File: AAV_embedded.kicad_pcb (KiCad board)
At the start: 4 copper layers, 168.2 x 114.7 mm, 84 parts, among them J1 JTAG_SWD_CONN, J10 DRV_HIGH_C2, J11 DRV_LOW_C2, J12 DRV_HIGH_C3, J13 DRV_LOW_C3, J14 DRV_LOW_C1, J15 Brake/FwRev, J16 5v_in, J17 3.3v_in, J18 12v_in, J2 Raspberry_Pi_4, J21 CAN, J23 5v_rail, J24 3.3v_rail, J25 12v_rail, J26 GND_rail, J27 12v_rail_f, J28 3.3v_rail_f, J29 5v_rail_f, J3 USB_C_Receptacle_USB2.0_14P, J30 GND_rail_f, J5 THR_EN_JMP, J6 Conn_01x07, J7 Conn_01x05, J8 Throttle Connector, J9 DRV_HIGH_C1, SW10 SW_DIP_x02, SW2 IO_EXT_ADDR, SW3 SW_DIP_x03, SW4 5v_USB_EN, SW5 THR_EN, SW6 ~{RESET_uMOD}, SW7 ~{BOOT_uMOD}, SW8 ~{RESET_BRK}, SW9 ~{RESET_STR}, U1 DAC101C081CIMK, U2 PCA9555D, U3 74AHC1G08, U5 FXMA108, U6 MCP2515-xSO, U7 SN65HVD230, Y1 16MHz

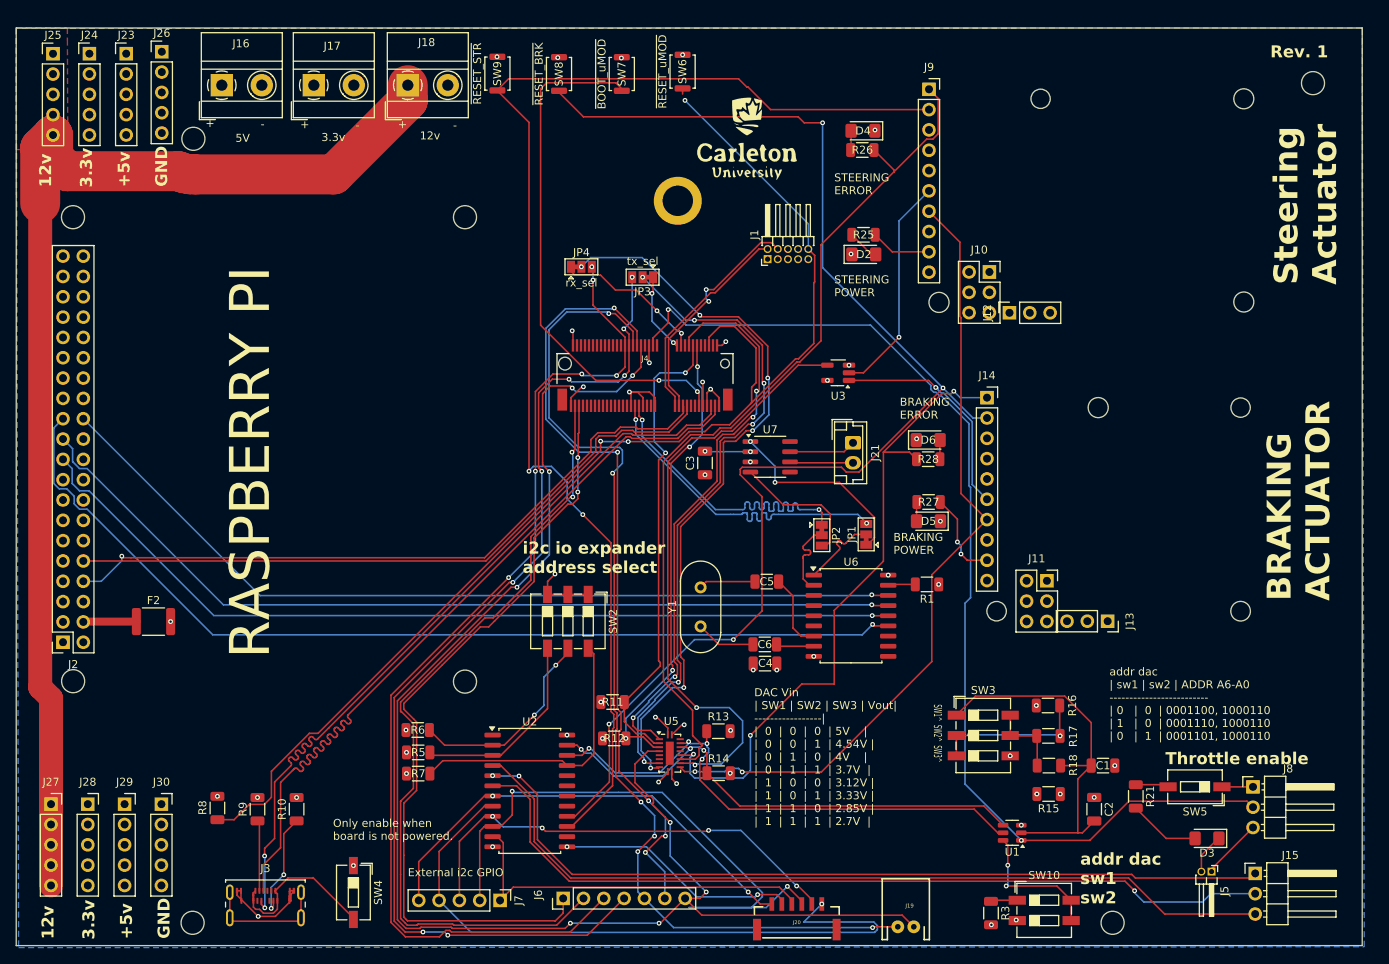
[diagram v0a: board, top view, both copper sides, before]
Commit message: Review and fixes from reliability and safety team
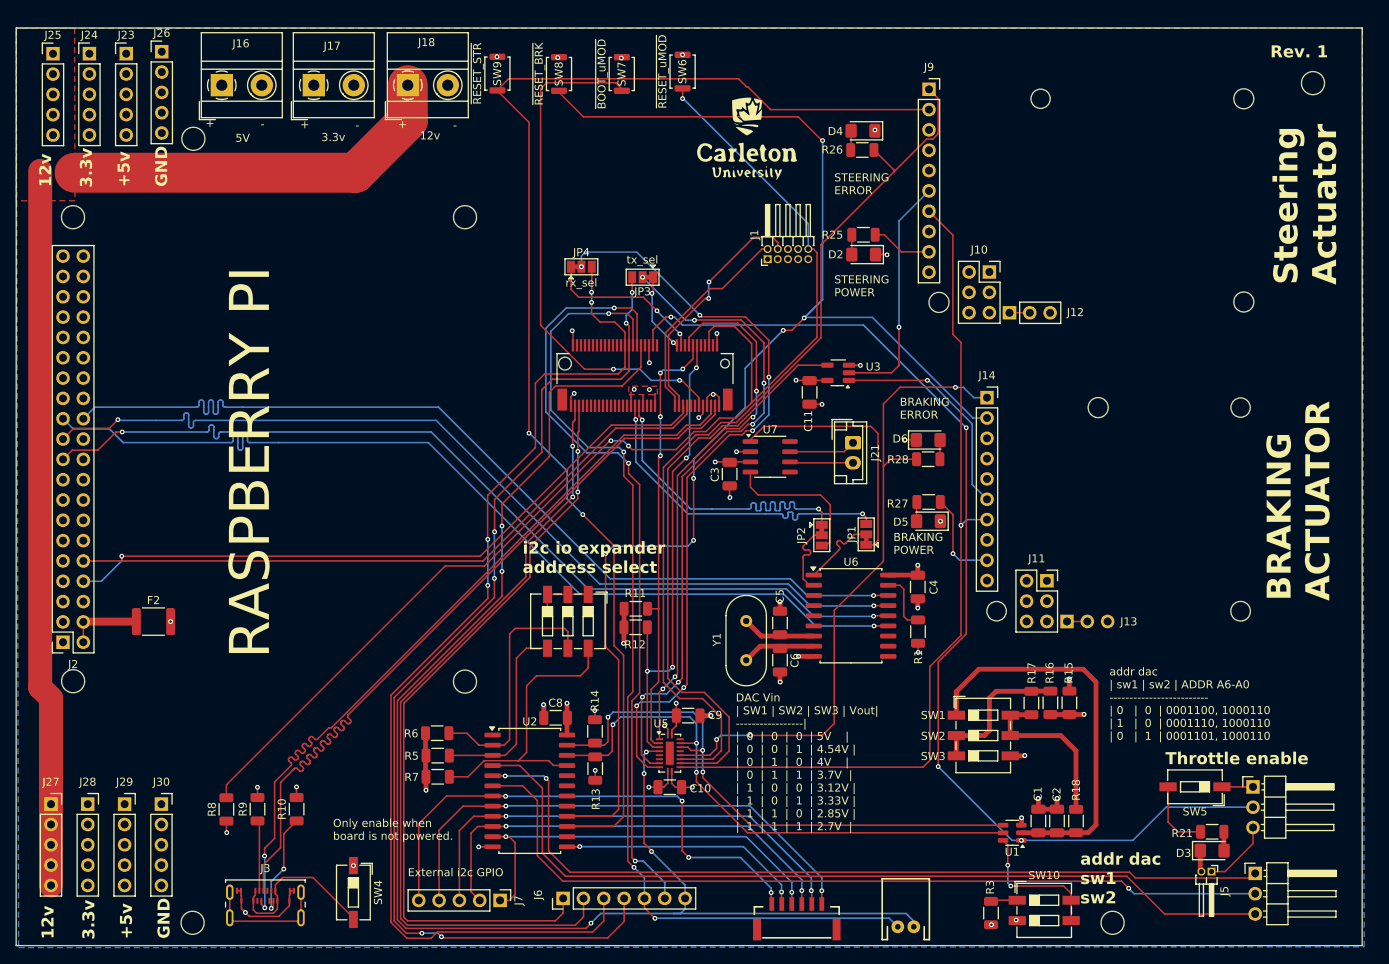
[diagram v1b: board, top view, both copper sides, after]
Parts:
- removed ?: , SparkFun-Hardware:STAND-OFF-REFLOW-M2.5
- added C10: 0.1uF, Capacitor_SMD:C_1206_3216Metric, F.Cu at (129.7, 138.1)
- added C11: 0.1uF, Capacitor_SMD:C_1206_3216Metric, F.Cu at (147.1, 88.7)
- added C8: 0.1uF, Capacitor_SMD:C_1206_3216Metric, F.Cu at (115.4, 129.4)
- added C9: 0.1uF, Capacitor_SMD:C_1206_3216Metric, F.Cu at (131.9, 129.1)
- Y1: footprint Crystal:Crystal_HC49-4H_Vertical -> Crystal:Crystal_HC18-U_Vertical
- moved C4 21.4 mm to (160.7, 113.0), turned to -90 degrees
- moved R14 16.3 mm to (120.3, 131.1), turned to 90 degrees
- moved R13 16.1 mm to (120.3, 135.7), turned to -90 degrees
- moved R12 14.1 mm to (125.4, 118.1)
- moved R11 12.0 mm to (125.4, 115.8)
- moved R15 11.7 mm to (179.6, 127.5), turned to -90 degrees
- moved C1 10.6 mm to (175.7, 142.3), turned to -90 degrees
- moved R21 10.5 mm to (197.4, 143.6), turned to 0 degrees
- moved R18 7.71 mm to (180.4, 142.3), turned to 90 degrees
- moved R1 6.01 mm to (160.7, 118.6), turned to 90 degrees
- moved Y1 5.74 mm to (139.2, 117.3), turned to -90 degrees
- moved C5 5.43 mm to (143.4, 117.5), turned to 90 degrees
- moved J13 5.08 mm to (179.3, 117.3), turned to 90 degrees
- moved C2 4.88 mm to (178.1, 142.3)
- moved R17 4.63 mm to (174.8, 127.5), turned to -90 degrees
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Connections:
- net Net-(D3-A) renamed /THR_STAT_K
- net Net-(D3-K) renamed /THR_STAT_A
- net Net-(R16-Pad1) renamed /SW2
- net Net-(R21-Pad1) renamed /THR_STAT_SW
- net Net-(U1-ADR0) renamed /DAC_ADR0
- net Net-(U2-A0) renamed /IO_EXP_A0
- net Net-(U2-A1) renamed /IO_EXP_A1
- net Net-(U2-A2) renamed /IO_EXP_A2
- net Net-(U6-~{RESET}) renamed /connectors/RESET
- C5 pad 1: Net-(U6-OSC2) -> /connectors/XTAL_2
- C5 pad 2: Net-(C5-Pad2) -> GND
- C6 pad 1: Net-(U6-OSC1) -> GND
- C6 pad 2: Net-(C6-Pad2) -> /connectors/XTAL_1
- R1 pad 1: GND -> +3.3V
- U6 pad 7: Net-(U6-OSC2) -> /connectors/XTAL_2
- U6 pad 8: Net-(U6-OSC1) -> /connectors/XTAL_1
- Y1 pad 1: Net-(C6-Pad2) -> /connectors/XTAL_2
- Y1 pad 2: Net-(C5-Pad2) -> /connectors/XTAL_1
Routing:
- net +5V: track 5.24 -> 29.5 mm, vias 15 -> 12
- net GPIO_EXT_3: track 79.7 -> 56.4 mm
- net GPIO_EXT_1: track 84.8 -> 65.7 mm, vias 1 -> 2
- net +3.3V: track 7.87 -> 25.3 mm, vias 11 -> 9
- net GND: track 51.0 -> 65.6 mm, vias 29 -> 34
- net Net-(R17-Pad2): track 9.61 -> 21.6 mm
- net +12V: track 149.9 -> 138.7 mm
- net Net-(U6-OSC2): track 9.56 -> 0.00 mm
- net /connectors/XTAL_2: track 0.00 -> 9.23 mm
- net /connectors/XTAL_1: track 0.00 -> 9.17 mm
- net CAN_CS: track 109.8 -> 118.3 mm
- net GPIO_EXT_0: track 58.0 -> 65.5 mm, vias 2 -> 4
- net Net-(C6-Pad2): track 7.48 -> 0.00 mm
- net Net-(JP1-A): track 24.9 -> 32.3 mm, vias 2 -> 0
- net RX_DRV_5v: track 99.9 -> 107.0 mm, vias 2 -> 1
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- added copper zone on F.Cu, net GND
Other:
- board text added: "SW1"
- board text added: "SW2"
- board text added: "SW3"
- board text removed: "SW1^ SW2^ SW3^"

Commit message: added micromod breakout and fixed voltage divider
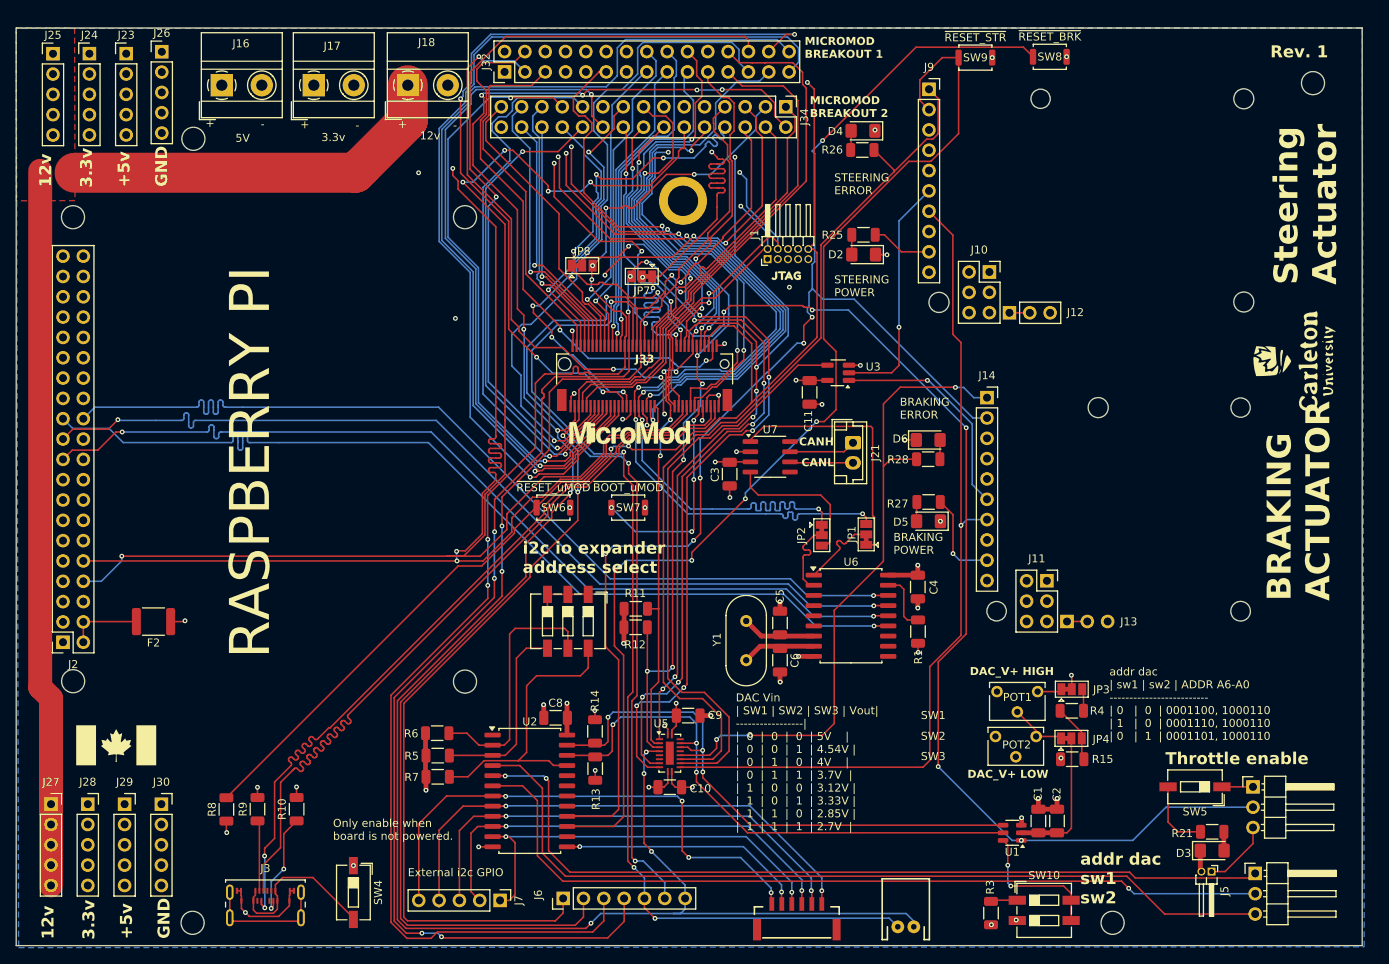
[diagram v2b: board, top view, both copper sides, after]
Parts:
- removed J4: ~, SparkFun-MicroMod:M.2-CONNECTOR-E
- removed R16: 10k, Resistor_SMD:R_1206_3216Metric
- removed R17: 5k, Resistor_SMD:R_1206_3216Metric
- removed R18: 2k, Resistor_SMD:R_1206_3216Metric
- removed SW3: SW_DIP_x03, Button_Switch_SMD:SW_DIP_SPSTx03_Slide_6.7x9.18mm_W6.73mm_P2.54mm_LowProfile_JPin
- added ?: , SparkFun-Buzzard:JTAG_TO, F.Cu at (141.4, 74.1)
- added ?: , SparkFun-Hardware:STAND-OFF-REFLOW-M2.5, F.Cu at (131.3, 64.8)
- added ?: , SparkFun-MicroMod:MICROMOD_LOGO_.6, F.Cu at (124.7, 93.8)
- added G***: LOGO, LOGO, F.Cu at (60.5, 132.8)
- added J32: Conn_02x15_Counter_Clockwise, Connector_PinHeader_2.54mm:PinHeader_2x15_P2.54mm_Vertical, F.Cu at (109.0, 48.6)
- added J33: ~, SparkFun-MicroMod:M.2-CONNECTOR-E, F.Cu at (126.5, 85.2)
- added J34: Conn_02x15_Counter_Clockwise, Connector_PinHeader_2.54mm:PinHeader_2x15_P2.54mm_Vertical, F.Cu at (144.2, 53.0)
- added JP7: tx_sel, Jumper:SolderJumper-3_P1.3mm_Bridged12_Pad1.0x1.5mm, F.Cu at (126.2, 74.2)
- added JP8: rx_sel, Jumper:SolderJumper-3_P1.3mm_Bridged12_Pad1.0x1.5mm, F.Cu at (118.7, 72.9)
- added POT1: TC33X-2-103E, Potentiometer_THT:Potentiometer_Bourns_3266W_Vertical, F.Cu at (175.6, 126.1)
- added POT2: TC33X-2-103E, Potentiometer_THT:Potentiometer_Bourns_3266W_Vertical, F.Cu at (175.4, 131.7)
- added R4: 10k, Resistor_SMD:R_1206_3216Metric, F.Cu at (179.9, 128.5)
- JP3: value tx_sel -> POT_HIGH_BYPASS
- JP4: value rx_sel -> POT_LOW_BYPASS
- moved JP4 85.0 mm to (179.8, 131.9)
- moved JP3 74.4 mm to (179.9, 125.8), turned to 0 degrees
- moved G*** 73.9 mm to (207.8, 84.8), turned to 90 degrees
- moved SW8 61.4 mm to (177.2, 46.8), turned to 180 degrees
- moved SW9 59.8 mm to (167.8, 46.9), turned to 180 degrees
- moved SW6 56.8 mm to (115.1, 103.1), turned to 180 degrees
- moved SW7 54.2 mm to (124.5, 103.1), turned to 180 degrees
- moved R15 7.06 mm to (179.9, 134.6), turned to 0 degrees
- turned F2 to 180 degrees
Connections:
- net DAC_THR renamed A0
- F2 pad 1: Net-(F2-Pad1) -> +5V
- F2 pad 2: +5V -> Net-(F2-Pad2)
- J2 pad 2: Net-(F2-Pad1) -> Net-(F2-Pad2)
- J2 pad 4: Net-(F2-Pad1) -> Net-(F2-Pad2)
- JP3 pad 2: TX_DRV_L -> +5V
- JP3 pad 3: GPIO_INTERNAL_3 -> Net-(JP3-B)
- JP4 pad 2: RX_DRV_L -> dac_v+
- JP4 pad 3: GPIO_INTERNAL_4 -> Net-(JP4-B)
- R15 pad 2: +5V -> Net-(JP4-B)
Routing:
- net I2C_SDA1: track 0.00 -> 120.5 mm, vias 0 -> 1
- net I2C_SCL1: track 0.00 -> 114.0 mm, vias 0 -> 1
- net BATT_VIN/3: track 0.00 -> 101.8 mm, vias 0 -> 4
- net G20/ADC_D/CAM_VSYNC: track 0.00 -> 98.5 mm, vias 0 -> 2
- net uMod_TX1: track 84.1 -> 179.8 mm, vias 0 -> 3
- net uMod_RX1: track 85.0 -> 177.7 mm, vias 1 -> 5
- net GPIO_INTERNAL_5: track 99.1 -> 189.6 mm, vias 2 -> 7
- net SPI_~{CS}: track 0.00 -> 85.9 mm, vias 0 -> 2
- net G9/ADC_D/CAM_HSYNC: track 0.00 -> 84.7 mm, vias 0 -> 1
- net USBHOST_D+: track 0.00 -> 83.8 mm, vias 0 -> 3
- net CAN_RXD: track 41.8 -> 117.6 mm, vias 2 -> 5
- net CAN_TXD: track 42.0 -> 117.0 mm, vias 2 -> 4
- net SPI_SCK: track 0.00 -> 74.7 mm, vias 0 -> 2
- net USBHOST_D-: track 0.00 -> 74.3 mm, vias 0 -> 3
- net SPI_SDI: track 0.00 -> 70.6 mm, vias 0 -> 1
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- removed copper zone on F.Cu, net GND
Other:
- board text added: "CANH"
- board text added: "CANL"
- board text added: "DAC_V+ HIGH"
- board text added: "DAC_V+ LOW"
- board text added: "MICROMOD BREAKOUT 1"
- board text added: "MICROMOD BREAKOUT 2"
